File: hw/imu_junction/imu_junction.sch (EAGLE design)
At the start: 58 parts, among them J1 JST-PH3SMT_VERT, J2 JST-PH3SMT_VERT, J3 JST-PH3SMT_VERT, J4 JST-PH3SMT_VERT, J5 JST-XH4SMT_RA, U1 STM32F4R_64PIN, U2 BMI088LGA16, U3 TPS62177WSON10, U4 MAX13431E, U5 MAX13431E, U6 MAX13431E, X1 8.0MHz

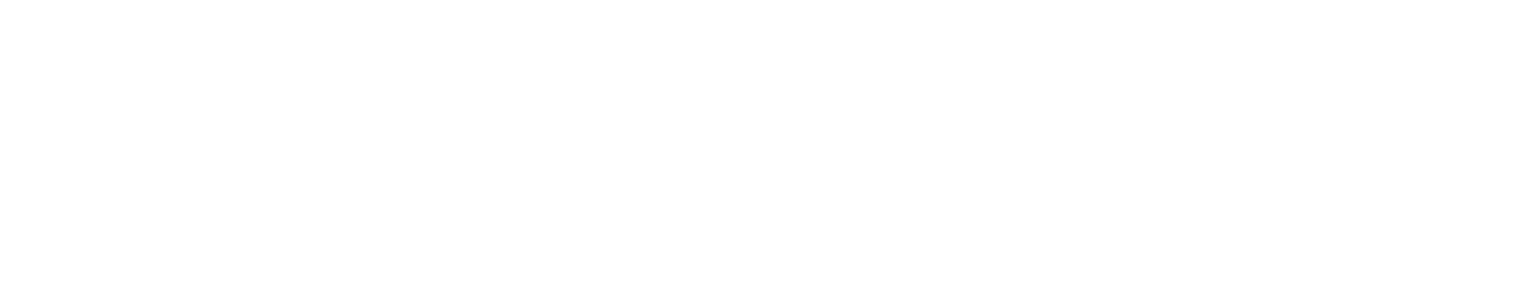
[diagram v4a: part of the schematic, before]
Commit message: imu_junction: Add copyright info to schematic
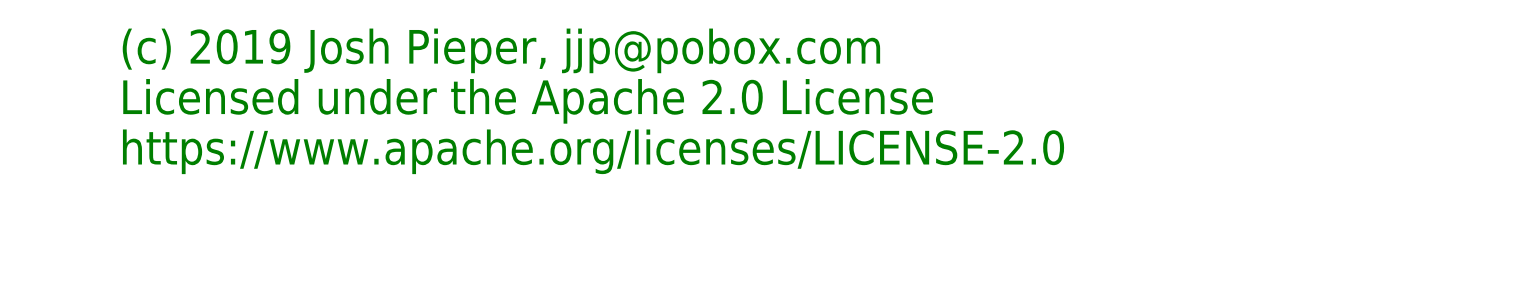
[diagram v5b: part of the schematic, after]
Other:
- note added: "(c) 2019 Josh Pieper, jjp@pobox.com Licensed under the Apache 2.0 License https://www.apache.org/licenses/LICENSE-2.0"
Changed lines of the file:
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@@
 <sheet>
 <plain>
+<text x="-50.8" y="175.26" size="5.08" layer="91">(c) 2019 Josh Pieper, jjp@pobox.com
+Licensed under the Apache 2.0 License
+https://www.apache.org/licenses/LICENSE-2.0</text>
 </plain>
 <instances>
@@
 </schematic>
 </drawing>
+<compatibility>
+<note version="6.3" minversion="6.2.2" severity="warning">
+Since Version 6.2.2 text objects can contain more than one line,
+which will not be processed correctly with this version.
+</note>
+</compatibility>
 </eagle>

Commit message: imu_junction r2
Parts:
- removed U$5: MOUNTM2, controller:MOUNTM2
- added C19: 10uF 35V, mfpassives:CAPACITOR_NP_1206
- added F1, F2: JST-PH2, imu_junction:JST-PH2
- added U7, U8: MF-DSC-SOT233-BSS138, mfdiscretesemi:N-CHANNEL_FET_BSS138_SOT-23-3
- C12: value 2.2uF 35V -> 10uF 35V; device mfpassives:CAPACITOR_NP_0603 -> mfpassives:CAPACITOR_NP_1206; MF Murata -> TDK; MPN GRM188R6YA225KA12D -> CGA5L1X7R1V106K160AC
- C13, C14: value 10uF -> 10uF 35V; HOUSEPART 1 -> (none); MF (none) -> TDK; MPN MF-CAP-1206-10uF -> CGA5L1X7R1V106K160AC
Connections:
- new net FAN1: U1.PA6/TIM3_1/SPI1_MISO/I2S2_MCK/TIM13_1, U7.GATE
- new net FAN2: U1.PA7/TIM1_1N/TIM3_2/TIM8_1N/SPI1_MOSI/I2S1_SD/TIM14_1, U8.GATE
- new net N$4: F1.2, U7.DRAIN
- new net N$9: F2.2, U8.DRAIN
- net +18V: now also C19.P$1, F1.1, F2.1
- net V-: now also C19.P$2, U7.SOURCE, U8.SOURCE
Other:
- moved on the sheet: C12
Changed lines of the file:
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@@
 <part name="P+1" library="supply1" deviceset="+18V" device=""/>
 <part name="+3V3" library="supply1" deviceset="+3V3" device=""/>
-<part name="C13" library="mfpassives" deviceset="CAPACITOR_NP" device="_1206" value="10uF">
-<attribute name="HOUSEPART" value="1"/>
-<attribute name="MPN" value="MF-CAP-1206-10uF"/>
-</part>
-<part name="C14" library="mfpassives" deviceset="CAPACITOR_NP" device="_1206" value="10uF">
-<attribute name="HOUSEPART" value="1"/>
-<attribute name="MPN" value="MF-CAP-1206-10uF"/>
-</part>
-<part name="C12" library="mfpassives" deviceset="CAPACITOR_NP" device="_0603" value="2.2uF 35V">
-<attribute name="MF" value="Murata"/>
-<attribute name="MPN" value="GRM188R6YA225KA12D"/>
+<part name="C13" library="mfpassives" deviceset="CAPACITOR_NP" device="_1206" value="10uF 35V">
+<attribute name="MF" value="TDK"/>
+<attribute name="MPN" value="CGA5L1X7R1V106K160AC"/>
+</part>
+<part name="C14" library="mfpassives" deviceset="CAPACITOR_NP" device="_1206" value="10uF 35V">
+<attribute name="MF" value="TDK"/>
+<attribute name="MPN" value="CGA5L1X7R1V106K160AC"/>
 </part>
 <part name="C15" library="mfpassives" deviceset="CAPACITOR_NP" device="_0402" value="0.1uF 50V">
@@
 <attribute name="POPULATE" value="0"/>
 </part>
-<part name="U$5" library="controller" deviceset="MOUNT" device="M2" value="MOUNTM2">
-<attribute name="POPULATE" value="0"/>
-</part>
 <part name="GND8" library="supply1" deviceset="GND" device=""/>
 <part name="D1" library="mfleds" deviceset="LED_SINGLE" device="-0603-RED" value="MF-LED-0603-RED"/>
@@
 </part>
 <part name="+3V7" library="supply1" deviceset="+3V3" device=""/>
+<part name="C19" library="mfpassives" deviceset="CAPACITOR_NP" device="_1206" value="10uF 35V">
+<attribute name="MF" value="TDK"/>
+<attribute name="MPN" value="CGA5L1X7R1V106K160AC"/>
+</part>
+<part name="C12" library="mfpassives" deviceset="CAPACITOR_NP" device="_1206" value="10uF 35V">
+<attribute name="MF" value="TDK"/>
+<attribute name="MPN" value="CGA5L1X7R1V106K160AC"/>
+</part>
+<part name="U7" library="mfdiscretesemi" deviceset="N-CHANNEL_FET" device="_SOT-23-3" technology="_BSS138" value="MF-DSC-SOT233-BSS138"/>
+<part name="U8" library="mfdiscretesemi" deviceset="N-CHANNEL_FET" device="_SOT-23-3" technology="_BSS138" value="MF-DSC-SOT233-BSS138"/>
+<part name="F1" library="imu_junction" deviceset="JST-PH2" device="">
+<attribute name="MF" value="JST"/>
+<attribute name="MPN" value="B2B-PH-SM4-TB(LF)(SN)"/>
+<attribute name="POPULATE" value="1"/>
+</part>
+<part name="F2" library="imu_junction" deviceset="JST-PH2" device="">
+<attribute name="MF" value="JST"/>
+<attribute name="MPN" value="B2B-PH-SM4-TB(LF)(SN)"/>
+<attribute name="POPULATE" value="1"/>
+</part>
+<part name="P+2" library="supply1" deviceset="+18V" device=""/>
+<part name="P+3" library="supply1" deviceset="+18V" device=""/>
 </parts>
 <sheets>
@@
 <instance part="P+1" gate="1" x="50.8" y="-274.32"/>
 <instance part="+3V3" gate="G$1" x="60.96" y="-289.56"/>
-<instance part="C13" gate="G$1" x="127" y="-297.18"/>
-<instance part="C14" gate="G$1" x="134.62" y="-297.18"/>
-<instance part="C12" gate="G$1" x="50.8" y="-299.72">
-<attribute name="MF" x="50.8" y="-299.72" size="1.778" layer="96" display="off"/>
+<instance part="C13" gate="G$1" x="127" y="-297.18">
+<attribute name="MF" x="127" y="-297.18" size="1.778" layer="96" display="off"/>
+</instance>
+<instance part="C14" gate="G$1" x="134.62" y="-297.18">
+<attribute name="MF" x="134.62" y="-297.18" size="1.778" layer="96" display="off"/>
 </instance>
 <instance part="C15" gate="G$1" x="144.78" y="-297.18">
@@
 <attribute name="POPULATE" x="-91.44" y="17.78" size="1.778" layer="96" rot="R180" display="off"/>
 </instance>
-<instance part="U$5" gate="G$1" x="50.8" y="124.46">
-<attribute name="POPULATE" x="50.8" y="124.46" size="1.778" layer="96" display="off"/>
-</instance>
 <instance part="GND8" gate="1" x="68.58" y="-215.9"/>
 <instance part="D1" gate="G$1" x="185.42" y="-86.36" rot="R270"/>
@@
 </instance>
 <instance part="+3V7" gate="G$1" x="195.58" y="-66.04"/>
+<instance part="C19" gate="G$1" x="48.26" y="-299.72">
+<attribute name="MF" x="48.26" y="-299.72" size="1.778" layer="96" display="off"/>
+</instance>
+<instance part="C12" gate="G$1" x="40.64" y="-299.72">
+<attribute name="MF" x="40.64" y="-299.72" size="1.778" layer="96" display="off"/>
+</instance>
+<instance part="U7" gate="G$1" x="195.58" y="-170.18"/>
+<instance part="U8" gate="G$1" x="256.54" y="-170.18"/>
+<instance part="F1" gate="A" x="190.5" y="-144.78">
+<attribute name="POPULATE" x="190.5" y="-144.78" size="1.778" layer="96" display="off"/>
+<attribute name="MPN" x="190.5" y="-144.78" size="1.778" layer="96" display="off"/>
+<attribute name="MF" x="190.5" y="-144.78" size="1.778" layer="96" display="off"/>
+</instance>
+<instance part="F2" gate="A" x="251.46" y="-147.32">
+<attribute name="POPULATE" x="251.46" y="-147.32" size="1.778" layer="96" display="off"/>
+<attribute name="MPN" x="251.46" y="-147.32" size="1.778" layer="96" display="off"/>
+<attribute name="MF" x="251.46" y="-147.32" size="1.778" layer="96" display="off"/>
+</instance>
+<instance part="P+2" gate="1" x="198.12" y="-129.54"/>
+<instance part="P+3" gate="1" x="259.08" y="-132.08"/>
 </instances>
 <busses>
@@
 <wire x1="50.8" y1="-281.94" x2="68.58" y2="-281.94" width="0.1524" layer="91"/>
 <junction x="68.58" y="-281.94"/>
+<pinref part="C19" gate="G$1" pin="P$1"/>
+<wire x1="50.8" y1="-281.94" x2="48.26" y2="-281.94" width="0.1524" layer="91"/>
+<wire x1="48.26" y1="-281.94" x2="48.26" y2="-297.18" width="0.1524" layer="91"/>
+<junction x="50.8" y="-281.94"/>
 <pinref part="C12" gate="G$1" pin="P$1"/>
-<wire x1="50.8" y1="-281.94" x2="50.8" y2="-297.18" width="0.1524" layer="91"/>
-<junction x="50.8" y="-281.94"/>
+<wire x1="48.26" y1="-281.94" x2="40.64" y2="-281.94" width="0.1524" layer="91"/>
+<wire x1="40.64" y1="-281.94" x2="40.64" y2="-297.18" width="0.1524" layer="91"/>
+<junction x="48.26" y="-281.94"/>
 </segment>
 <segment>
@@
 <label x="119.38" y="-480.06" size="1.778" layer="95"/>
 </segment>
+<segment>
+<pinref part="F1" gate="A" pin="1"/>
+<pinref part="P+2" gate="1" pin="+18V"/>
+<wire x1="195.58" y1="-142.24" x2="198.12" y2="-142.24" width="0.1524" layer="91"/>
+<wire x1="198.12" y1="-142.24" x2="198.12" y2="-132.08" width="0.1524" layer="91"/>
+</segment>
+<segment>
+<pinref part="F2" gate="A" pin="1"/>
+<pinref part="P+3" gate="1" pin="+18V"/>
+<wire x1="256.54" y1="-144.78" x2="259.08" y2="-144.78" width="0.1524" layer="91"/>
+<wire x1="259.08" y1="-144.78" x2="259.08" y2="-134.62" width="0.1524" layer="91"/>
+</segment>
 </net>
 <net name="D2_P" class="0">
@@
 <junction x="71.12" y="-307.34"/>
 <wire x1="71.12" y1="-307.34" x2="71.12" y2="-314.96" width="0.1524" layer="91"/>
-<pinref part="C12" gate="G$1" pin="P$2"/>
-<wire x1="50.8" y1="-302.26" x2="50.8" y2="-314.96" width="0.1524" layer="91"/>
-<wire x1="50.8" y1="-314.96" x2="71.12" y2="-314.96" width="0.1524" layer="91"/>
+<wire x1="48.26" y1="-314.96" x2="71.12" y2="-314.96" width="0.1524" layer="91"/>
 <wire x1="71.12" y1="-314.96" x2="71.12" y2="-317.5" width="0.1524" layer="91"/>
 <junction x="71.12" y="-314.96"/>
@@
 <wire x1="71.12" y1="-325.12" x2="86.36" y2="-325.12" width="0.1524" layer="91"/>
 <junction x="71.12" y="-325.12"/>
+<pinref part="C19" gate="G$1" pin="P$2"/>
+<wire x1="48.26" y1="-314.96" x2="48.26" y2="-302.26" width="0.1524" layer="91"/>
+<pinref part="C12" gate="G$1" pin="P$2"/>
+<wire x1="48.26" y1="-314.96" x2="40.64" y2="-314.96" width="0.1524" layer="91"/>
+<wire x1="40.64" y1="-314.96" x2="40.64" y2="-302.26" width="0.1524" layer="91"/>
+<junction x="48.26" y="-314.96"/>
 </segment>
 <segment>
@@
 <label x="86.36" y="-441.96" size="1.778" layer="95"/>
 </segment>
+<segment>
+<pinref part="U7" gate="G$1" pin="SOURCE"/>
+<wire x1="198.12" y1="-177.8" x2="198.12" y2="-180.34" width="0.1524" layer="91"/>
+<pinref part="U8" gate="G$1" pin="SOURCE"/>
+<wire x1="259.08" y1="-177.8" x2="259.08" y2="-180.34" width="0.1524" layer="91"/>
+<wire x1="259.08" y1="-180.34" x2="259.08" y2="-182.88" width="0.1524" layer="91"/>
+<wire x1="198.12" y1="-180.34" x2="259.08" y2="-180.34" width="0.1524" layer="91"/>
+<junction x="259.08" y="-180.34"/>
+<label x="261.62" y="-182.88" size="1.778" layer="95"/>
+</segment>
 </net>
 <net name="TX3" class="0">
@@
 </segment>
 </net>
+<net name="FAN1" class="0">
+<segment>
+<pinref part="U7" gate="G$1" pin="GATE"/>
+<wire x1="187.96" y1="-170.18" x2="165.1" y2="-170.18" width="0.1524" layer="91"/>
+<label x="165.1" y="-170.18" size="1.778" layer="95"/>
+</segment>
+<segment>
+<pinref part="U1" gate="G$1" pin="PA6/TIM3_1/SPI1_MISO/I2S2_MCK/TIM13_1"/>
+<wire x1="5.08" y1="30.48" x2="-17.78" y2="30.48" width="0.1524" layer="91"/>
+<label x="-17.78" y="30.48" size="1.778" layer="95"/>
+</segment>
+</net>
+<net name="FAN2" class="0">
+<segment>
+<pinref part="U8" gate="G$1" pin="GATE"/>
+<wire x1="248.92" y1="-170.18" x2="228.6" y2="-170.18" width="0.1524" layer="91"/>
+<label x="228.6" y="-167.64" size="1.778" layer="95"/>
+</segment>
+<segment>
+<pinref part="U1" gate="G$1" pin="PA7/TIM1_1N/TIM3_2/TIM8_1N/SPI1_MOSI/I2S1_SD/TIM14_1"/>
+<wire x1="5.08" y1="27.94" x2="-17.78" y2="27.94" width="0.1524" layer="91"/>
+<label x="-17.78" y="27.94" size="1.778" layer="95"/>
+</segment>
+</net>
+<net name="N$4" class="0">
+<segment>
+<pinref part="F1" gate="A" pin="2"/>
+<pinref part="U7" gate="G$1" pin="DRAIN"/>
+<wire x1="195.58" y1="-144.78" x2="198.12" y2="-144.78" width="0.1524" layer="91"/>
+<wire x1="198.12" y1="-144.78" x2="198.12" y2="-162.56" width="0.1524" layer="91"/>
+</segment>
+</net>
+<net name="N$9" class="0">
+<segment>
+<pinref part="F2" gate="A" pin="2"/>
+<pinref part="U8" gate="G$1" pin="DRAIN"/>
+<wire x1="256.54" y1="-147.32" x2="259.08" y2="-147.32" width="0.1524" layer="91"/>
+<wire x1="259.08" y1="-147.32" x2="259.08" y2="-162.56" width="0.1524" layer="91"/>
+</segment>
+</net>

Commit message: Work towards an r3 of the imu junction board
Decided that I can probably live for now with just an anti-spark
connector on the battery.  I hadn't decided how to handle the common
mode ground shift on the RS485 bus with a switched ground system
during the startup transient.
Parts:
- removed DGND, DRX, DTX: PAD24AWG_PAD, controller:PAD24AWG_PAD
- added C20: 10uF 35V, mfpassives:CAPACITOR_NP_1206
- added C21, C22, C23: 0.1uF 50V, mfpassives:CAPACITOR_NP_0402
- added D3: (no value), imu_junction:DIODE-
- added R4: 10 1W, mfpassives:RESISTOR_1206
- added U$10, U$8, U$9: MIC4416, imu_junction:MIC4416
- added U$11: ZXTR2012Z, imu_junction:ZXTR2012Z
- added U$12: SLIDE_SWITCHJS_SUB_SWITCH, imu_junction:SLIDE_SWITCHJS_SUB_SWITCH
- added U$5, U$6, U$7: TPH1R204PL, imu_junction:TPH1R204PL
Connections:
- removed net N$3: DRX.P$1, U1.PA10/TIM1_3/USART1_RX
- new net +12V: C20.P$1, C21.P$1, C22.P$1, C23.P$1, U$10.VS, U$11.VOUT, U$8.VS, U$9.VS
- new net N$10: R4.P$1, U$5.D
- new net N$11: U$6.G, U$9.G
- new net N$12: U$5.G, U$8.G
- new net N$13: U$10.G, U$7.G
- new net PWR_CPU: U$10.CTL
- new net PWR_MOTOR: U$9.CTL
- new net PWR_PRECHARGE: U$8.CTL
- new net V-CPU: J5.1, U$7.D
- new net V-MOTOR: D3.A, J1.3, J2.3, J3.3, J4.3, R4.P$2, U$6.D
- net +18V: now also D3.C, U$11.VIN
- net GND: now also C20.P$2, C21.P$2, C22.P$2, C23.P$2, U$10.GND, U$11.GND, U$12.3, U$8.GND, U$9.GND; no longer DGND.P$1
- net N$2: now also U$12.2, U1.PC0; no longer DTX.P$1, U1.PA9/TIM1_2/SPI2_SCK/I2S3_CK/UART1_TX/USB_VBUS
- net V-: now also U$5.S, U$6.S, U$7.S; no longer J1.3, J2.3, J3.3, J4.3, J5.1
